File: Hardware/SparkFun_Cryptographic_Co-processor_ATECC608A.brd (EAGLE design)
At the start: 25.4 x 25.4 mm, 41 parts, among them J1 QWIIC, J2 QWIIC, J3 PTH, U1 ATECC608A

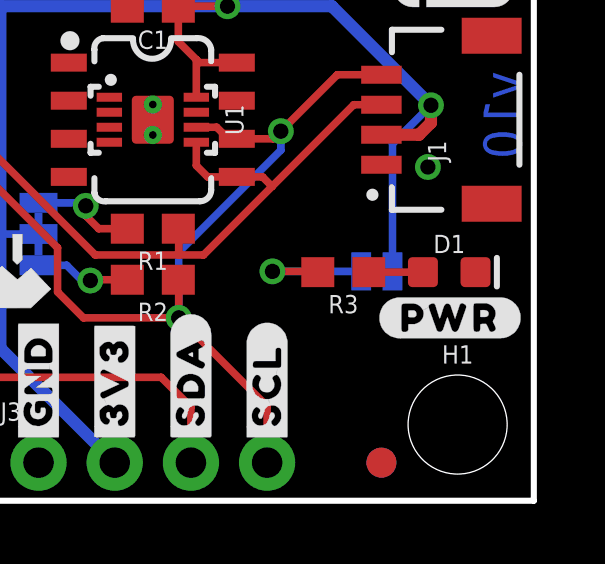
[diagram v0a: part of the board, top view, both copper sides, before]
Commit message: PWR to text only buzzard (was previously inverted bubble)
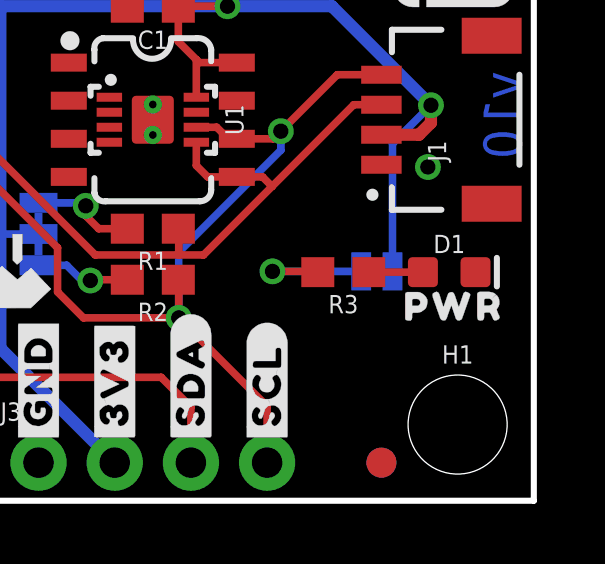
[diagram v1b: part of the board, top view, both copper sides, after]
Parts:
- removed U$14: (no value), output:#PWR#0
- added U$11: (no value), output:PWR0
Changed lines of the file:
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@@
 <setting verticaltext="up"/>
 </settings>
-<grid distance="0.05" unitdist="inch" unit="inch" style="lines" multiple="1" display="yes" altdistance="0.001" altunitdist="inch" altunit="inch"/>
+<grid distance="0.05" unitdist="inch" unit="inch" style="lines" multiple="1" display="yes" altdistance="0.005" altunitdist="inch" altunit="inch"/>
 <layers>
 <layer number="1" name="Top" color="4" fill="1" visible="yes" active="yes"/>
@@
 <layer number="27" name="tValues" color="7" fill="1" visible="no" active="yes"/>
 <layer number="28" name="bValues" color="7" fill="1" visible="no" active="yes"/>
-<layer number="29" name="tStop" color="7" fill="3" visible="no" active="yes"/>
+<layer number="29" name="tStop" color="7" fill="3" visible="yes" active="yes"/>
 <layer number="30" name="bStop" color="7" fill="6" visible="no" active="yes"/>
 <layer number="31" name="tCream" color="7" fill="4" visible="no" active="yes"/>
@@
 <layer number="47" name="Measures" color="7" fill="1" visible="no" active="yes"/>
 <layer number="48" name="Document" color="7" fill="1" visible="no" active="yes"/>
-<layer number="49" name="Reference" color="13" fill="1" visible="yes" active="yes"/>
+<layer number="49" name="Reference" color="13" fill="1" visible="no" active="yes"/>
 <layer number="50" name="dxf" color="7" fill="1" visible="no" active="yes"/>
 <layer number="51" name="tDocu" color="6" fill="1" visible="yes" active="yes"/>
@@
 <element name="U$9" library="output" package="CRYPTOGRAPHIC_CO#PROCESSOR0" value="" x="12.8524" y="19.4818" smashed="yes"/>
 <element name="U$19" library="output" package="CRYPTOGRAPHIC_CO#PROCESSOR0" value="" x="12.7254" y="19.4818" smashed="yes" rot="MR0"/>
-<element name="U$14" library="output" package="#PWR#0" value="" x="22.606" y="6.096" smashed="yes"/>
 <element name="U$13" library="output" package="#SCL#0" value="" x="16.51" y="1.778" smashed="yes" rot="R90"/>
 <element name="U$17" library="output" package="#SDA#0" value="" x="13.97" y="1.778" smashed="yes" rot="R90"/>
@@
 <element name="U$10" library="SparkFun-Aesthetics" package="CRYPTO_COPROCESSOR_LOGO_SMALL" value="" x="5.207" y="7.112" smashed="yes"/>
 <element name="LOGO3" library="SparkFun-Aesthetics" package="QWIIC_4MM" value="QWIIC_LOGO_4MM" x="22.733" y="17.0942" smashed="yes"/>
+<element name="U$11" library="output" package="PWR0" value="" x="22.733" y="6.477" smashed="yes"/>
 </elements>
 <signals>
